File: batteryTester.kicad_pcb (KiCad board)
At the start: 2 copper layers, 65 x 78 mm, 41 parts, among them J1 OLED_DISPLAY, J2 USB_C_Receptacle_USB2.0_16P, J3 PROG, Q1 IRF540N, SW1 START, SW2 STOP, SW3 STOP, U1 AMS1117-3.3, U2 LMV321, U3 LMV321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

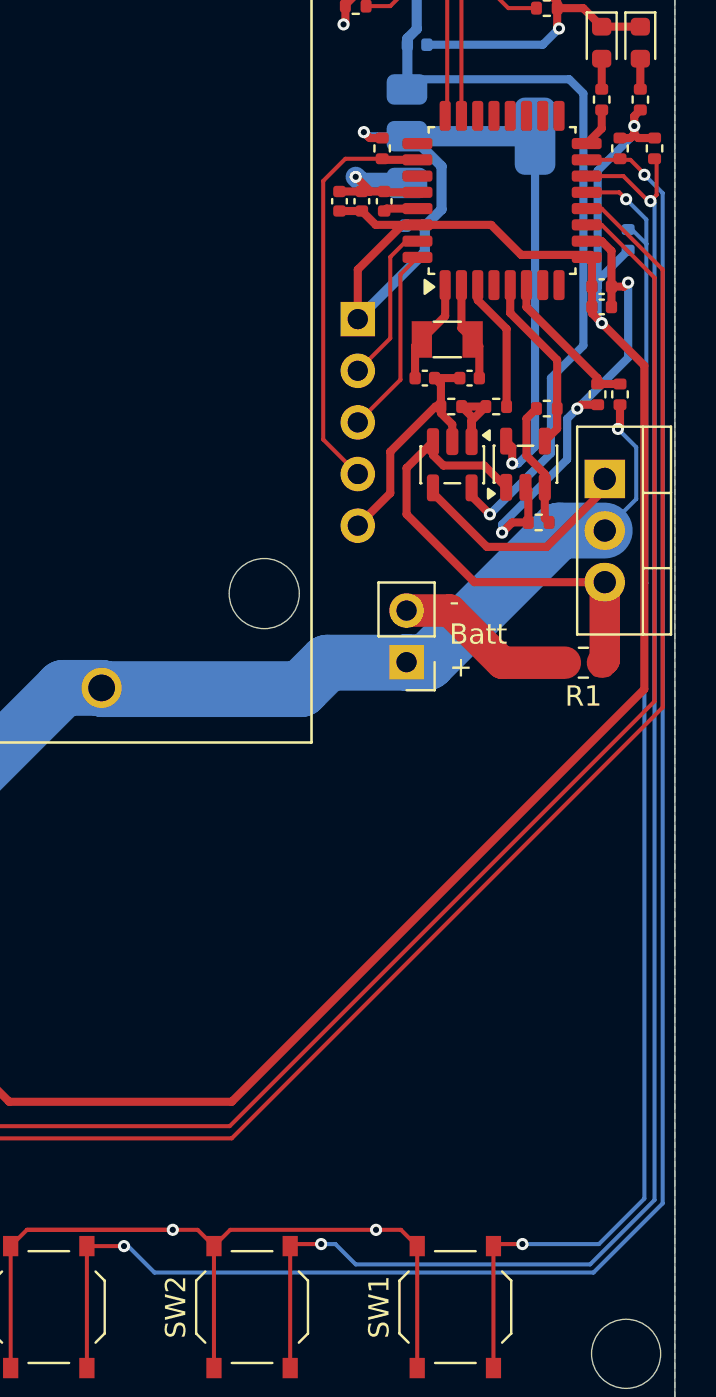
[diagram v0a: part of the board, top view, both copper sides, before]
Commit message: add i2c pullups
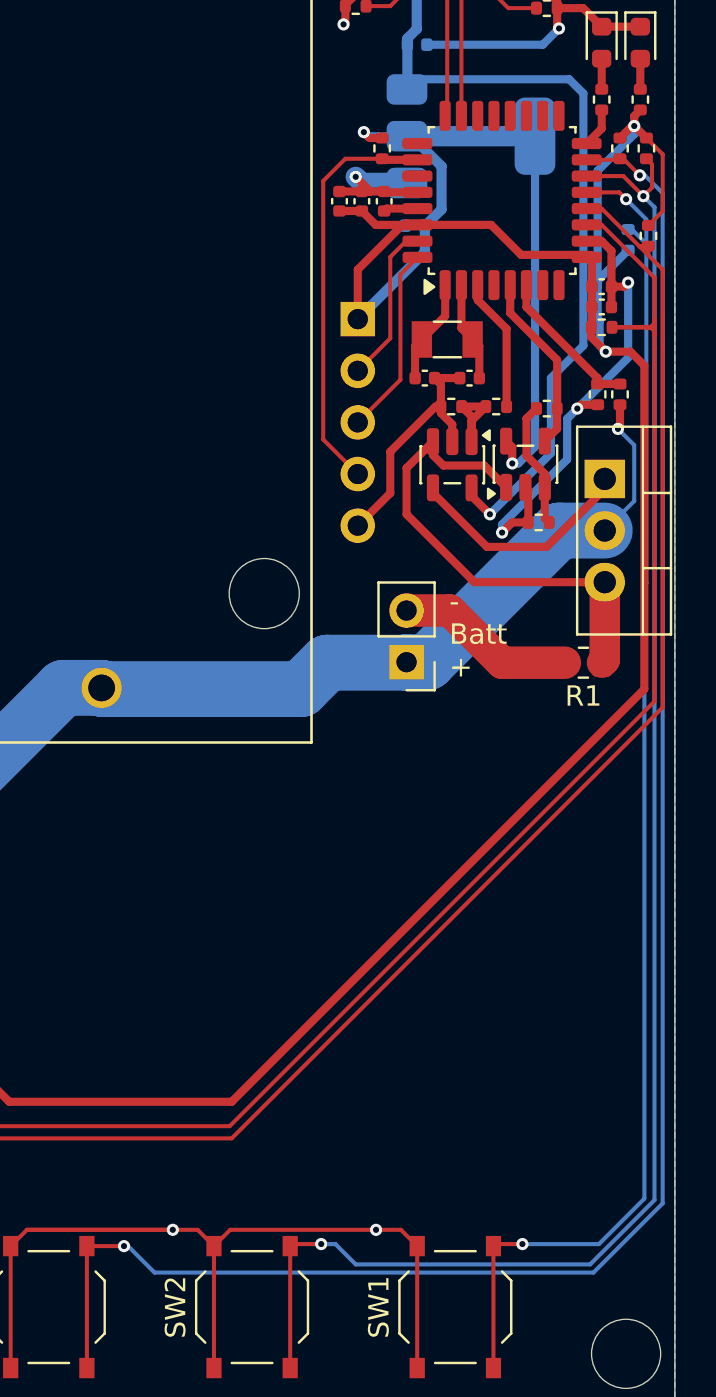
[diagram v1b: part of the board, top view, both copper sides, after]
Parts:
- added R16: 4.7k, Resistor_SMD:R_0402_1005Metric, F.Cu at (156.5, 80.8)
- added R17: 4.7k, Resistor_SMD:R_0402_1005Metric, F.Cu at (154.2, 85.3)
- moved R9 0.40 mm to (156.4, 76.5)
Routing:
- net +3.3V: track 142.3 -> 148.9 mm
- net SDA: track 69.5 -> 74.7 mm
- net SCL: track 78.2 -> 79.1 mm
